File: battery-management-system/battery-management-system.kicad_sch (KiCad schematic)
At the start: 0 parts

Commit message: improve placement
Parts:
- added H1, H2, H3, H4: MountingHole_Pad, MountingHole:MountingHole_6.4mm_M6_Pad, symbol benediktibk:MountingHole_Pad_M6
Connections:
- new net GND: H1.1, H2.1, H3.1, H4.1
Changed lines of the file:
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@@
   (junction (at 68.58 91.44) (diameter 0) (color 0 0 0 0)
   )
+  (wire (pts (xy 236.22 40.64) (xy 236.22 41.91))
+    (stroke (width 0) (type default))
+  )
   (wire (pts (xy 58.42 87.63) (xy 71.12 87.63))
     (stroke (width 0) (type default))
@@
     (stroke (width 0) (type default))
   )
+  (wire (pts (xy 259.08 25.4) (xy 259.08 26.67))
+    (stroke (width 0) (type default))
+  )
   (wire (pts (xy 12.7 83.82) (xy 22.86 83.82))
     (stroke (width 0) (type default))
@@
     (stroke (width 0) (type default))
   )
+  (wire (pts (xy 259.08 40.64) (xy 259.08 41.91))
+    (stroke (width 0) (type default))
+  )
   (wire (pts (xy 78.74 130.81) (xy 106.68 130.81))
     (stroke (width 0) (type default))
@@
     (stroke (width 0) (type default))
   )
+  (wire (pts (xy 236.22 25.4) (xy 236.22 26.67))
+    (stroke (width 0) (type default))
+  )
   (wire (pts (xy 195.58 87.63) (xy 242.57 87.63))
     (stroke (width 0) (type default))
@@
     (effects (font (size 1.27 1.27)) (justify left bottom))
   )
+  (symbol (lib_id "power:GND") (at 236.22 41.91 0) (unit 1)
+    (in_bom yes) (on_board yes) (dnp no) (fields_autoplaced)
+    (property "Reference" "#PWR045" (at 236.22 48.26 0)
+      (effects (font (size 1.27 1.27)) hide)
+    )
+    (property "Value" "GND" (at 236.22 46.99 0)
+      (effects (font (size 1.27 1.27)))
+    )
+    (property "Footprint" "" (at 236.22 41.91 0)
+      (effects (font (size 1.27 1.27)) hide)
+    )
+    (property "Datasheet" "" (at 236.22 41.91 0)
+      (effects (font (size 1.27 1.27)) hide)
+    )
+    (pin "1")
+    (instances
+      (project "battery-management-system"
+        (path "/5272f0ff-3069-41a9-bca2-80beede8b4b2"
+          (reference "#PWR045") (unit 1)
+        )
+      )
+    )
+  )
+  (symbol (lib_id "power:GND") (at 259.08 41.91 0) (unit 1)
+    (in_bom yes) (on_board yes) (dnp no) (fields_autoplaced)
+    (property "Reference" "#PWR047" (at 259.08 48.26 0)
+      (effects (font (size 1.27 1.27)) hide)
+    )
+    (property "Value" "GND" (at 259.08 46.99 0)
+      (effects (font (size 1.27 1.27)))
+    )
+    (property "Footprint" "" (at 259.08 41.91 0)
+      (effects (font (size 1.27 1.27)) hide)
+    )
+    (property "Datasheet" "" (at 259.08 41.91 0)
+      (effects (font (size 1.27 1.27)) hide)
+    )
+    (pin "1")
+    (instances
+      (project "battery-management-system"
+        (path "/5272f0ff-3069-41a9-bca2-80beede8b4b2"
+          (reference "#PWR047") (unit 1)
+        )
+      )
+    )
+  )
+  (symbol (lib_id "benediktibk:MountingHole_Pad_M6") (at 259.08 22.86 0) (unit 1)
+    (in_bom yes) (on_board yes) (dnp no) (fields_autoplaced)
+    (property "Reference" "H3" (at 261.62 20.32 0)
+      (effects (font (size 1.27 1.27)) (justify left))
+    )
+    (property "Value" "MountingHole_Pad" (at 261.62 22.86 0)
+      (effects (font (size 1.27 1.27)) (justify left))
+    )
+    (property "Footprint" "MountingHole:MountingHole_6.4mm_M6_Pad" (at 259.08 22.86 0)
+      (effects (font (size 1.27 1.27)) hide)
+    )
+    (property "Datasheet" "~" (at 259.08 22.86 0)
+      (effects (font (size 1.27 1.27)) hide)
+    )
+    (pin "1")
+    (instances
+      (project "battery-management-system"
+        (path "/5272f0ff-3069-41a9-bca2-80beede8b4b2"
+          (reference "H3") (unit 1)
+        )
+      )
+    )
+  )
+  (symbol (lib_id "benediktibk:MountingHole_Pad_M6") (at 236.22 22.86 0) (unit 1)
+    (in_bom yes) (on_board yes) (dnp no) (fields_autoplaced)
+    (property "Reference" "H1" (at 238.76 20.32 0)
+      (effects (font (size 1.27 1.27)) (justify left))
+    )
+    (property "Value" "MountingHole_Pad" (at 238.76 22.86 0)
+      (effects (font (size 1.27 1.27)) (justify left))
+    )
+    (property "Footprint" "MountingHole:MountingHole_6.4mm_M6_Pad" (at 236.22 22.86 0)
+      (effects (font (size 1.27 1.27)) hide)
+    )
+    (property "Datasheet" "~" (at 236.22 22.86 0)
+      (effects (font (size 1.27 1.27)) hide)
+    )
+    (pin "1")
+    (instances
+      (project "battery-management-system"
+        (path "/5272f0ff-3069-41a9-bca2-80beede8b4b2"
+          (reference "H1") (unit 1)
+        )
+      )
+    )
+  )
+  (symbol (lib_id "power:GND") (at 236.22 26.67 0) (unit 1)
+    (in_bom yes) (on_board yes) (dnp no) (fields_autoplaced)
+    (property "Reference" "#PWR044" (at 236.22 33.02 0)
+      (effects (font (size 1.27 1.27)) hide)
+    )
+    (property "Value" "GND" (at 236.22 31.75 0)
+      (effects (font (size 1.27 1.27)))
+    )
+    (property "Footprint" "" (at 236.22 26.67 0)
+      (effects (font (size 1.27 1.27)) hide)
+    )
+    (property "Datasheet" "" (at 236.22 26.67 0)
+      (effects (font (size 1.27 1.27)) hide)
+    )
+    (pin "1")
+    (instances
+      (project "battery-management-system"
+        (path "/5272f0ff-3069-41a9-bca2-80beede8b4b2"
+          (reference "#PWR044") (unit 1)
+        )
+      )
+    )
+  )
+  (symbol (lib_id "benediktibk:MountingHole_Pad_M6") (at 259.08 38.1 0) (unit 1)
+    (in_bom yes) (on_board yes) (dnp no) (fields_autoplaced)
+    (property "Reference" "H4" (at 261.62 35.56 0)
+      (effects (font (size 1.27 1.27)) (justify left))
+    )
+    (property "Value" "MountingHole_Pad" (at 261.62 38.1 0)
+      (effects (font (size 1.27 1.27)) (justify left))
+    )
+    (property "Footprint" "MountingHole:MountingHole_6.4mm_M6_Pad" (at 259.08 38.1 0)
+      (effects (font (size 1.27 1.27)) hide)
+    )
+    (property "Datasheet" "~" (at 259.08 38.1 0)
+      (effects (font (size 1.27 1.27)) hide)
+    )
+    (pin "1")
+    (instances
+      (project "battery-management-system"
+        (path "/5272f0ff-3069-41a9-bca2-80beede8b4b2"
+          (reference "H4") (unit 1)
+        )
+      )
+    )
+  )
+  (symbol (lib_id "benediktibk:MountingHole_Pad_M6") (at 236.22 38.1 0) (unit 1)
+    (in_bom yes) (on_board yes) (dnp no) (fields_autoplaced)
+    (property "Reference" "H2" (at 238.76 35.56 0)
+      (effects (font (size 1.27 1.27)) (justify left))
+    )
+    (property "Value" "MountingHole_Pad" (at 238.76 38.1 0)
+      (effects (font (size 1.27 1.27)) (justify left))
+    )
+    (property "Footprint" "MountingHole:MountingHole_6.4mm_M6_Pad" (at 236.22 38.1 0)
+      (effects (font (size 1.27 1.27)) hide)
+    )
+    (property "Datasheet" "~" (at 236.22 38.1 0)
+      (effects (font (size 1.27 1.27)) hide)
+    )
+    (pin "1")
+    (instances
+      (project "battery-management-system"
+        (path "/5272f0ff-3069-41a9-bca2-80beede8b4b2"
+          (reference "H2") (unit 1)
+        )
+      )
+    )
+  )
+  (symbol (lib_id "power:GND") (at 259.08 26.67 0) (unit 1)
+    (in_bom yes) (on_board yes) (dnp no) (fields_autoplaced)
+    (property "Reference" "#PWR046" (at 259.08 33.02 0)
+      (effects (font (size 1.27 1.27)) hide)
+    )
+    (property "Value" "GND" (at 259.08 31.75 0)
+      (effects (font (size 1.27 1.27)))
+    )
+    (property "Footprint" "" (at 259.08 26.67 0)
+      (effects (font (size 1.27 1.27)) hide)
+    )
+    (property "Datasheet" "" (at 259.08 26.67 0)
+      (effects (font (size 1.27 1.27)) hide)
+    )
+    (pin "1")
+    (instances
+      (project "battery-management-system"
+        (path "/5272f0ff-3069-41a9-bca2-80beede8b4b2"
+          (reference "#PWR046") (unit 1)
+        )
+      )
+    )
+  )
   (sheet (at 22.86 81.28) (size 35.56 27.94) (fields_autoplaced)

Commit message: finish first draft of layout
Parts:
- removed H4: MountingHole_Pad, MountingHole:MountingHole_6.4mm_M6_Pad, symbol benediktibk:MountingHole_Pad_M6
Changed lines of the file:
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@@
-    (stroke (width 0) (type default))
-  )
-  (wire (pts (xy 259.08 40.64) (xy 259.08 41.91))
     (stroke (width 0) (type default))
   )
@@
     )
   )
-  (symbol (lib_id "power:GND") (at 259.08 41.91 0) (unit 1)
-    (in_bom yes) (on_board yes) (dnp no) (fields_autoplaced)
-    (property "Reference" "#PWR047" (at 259.08 48.26 0)
-      (effects (font (size 1.27 1.27)) hide)
-    )
-    (property "Value" "GND" (at 259.08 46.99 0)
-      (effects (font (size 1.27 1.27)))
-    )
-    (property "Footprint" "" (at 259.08 41.91 0)
-      (effects (font (size 1.27 1.27)) hide)
-    )
-    (property "Datasheet" "" (at 259.08 41.91 0)
-      (effects (font (size 1.27 1.27)) hide)
-    )
-    (pin "1")
-    (instances
-      (project "battery-management-system"
-        (path "/5272f0ff-3069-41a9-bca2-80beede8b4b2"
-          (reference "#PWR047") (unit 1)
-        )
-      )
-    )
-  )
   (symbol (lib_id "benediktibk:MountingHole_Pad_M6") (at 259.08 22.86 0) (unit 1)
     (in_bom yes) (on_board yes) (dnp no) (fields_autoplaced)
@@
         )
       )
-    )
-  )
-  (symbol (lib_id "benediktibk:MountingHole_Pad_M6") (at 259.08 38.1 0) (unit 1)
-    (in_bom yes) (on_board yes) (dnp no) (fields_autoplaced)
-    (property "Reference" "H4" (at 261.62 35.56 0)
-      (effects (font (size 1.27 1.27)) (justify left))
-    )
-    (property "Value" "MountingHole_Pad" (at 261.62 38.1 0)
-      (effects (font (size 1.27 1.27)) (justify left))
-    )
-    (property "Footprint" "MountingHole:MountingHole_6.4mm_M6_Pad" (at 259.08 38.1 0)
-      (effects (font (size 1.27 1.27)) hide)
-    )
-    (property "Datasheet" "~" (at 259.08 38.1 0)
-      (effects (font (size 1.27 1.27)) hide)
-    )
-    (pin "1")
-    (instances
-      (project "battery-management-system"
-        (path "/5272f0ff-3069-41a9-bca2-80beede8b4b2"
-          (reference "H4") (unit 1)
-        )
-      )

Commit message: improve layout
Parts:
- H1, H2, H3: footprint MountingHole:MountingHole_6.4mm_M6_Pad -> benediktibk:MountingHole_6.4mm_M6_Pad_TopBottom
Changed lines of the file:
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@@
   (symbol (lib_id "power:GND") (at 236.22 41.91 0) (unit 1)
     (in_bom yes) (on_board yes) (dnp no) (fields_autoplaced)
-    (property "Reference" "#PWR045" (at 236.22 48.26 0)
+    (property "Reference" "#PWR02" (at 236.22 48.26 0)
       (effects (font (size 1.27 1.27)) hide)
     )
@@
       (project "battery-management-system"
         (path "/5272f0ff-3069-41a9-bca2-80beede8b4b2"
-          (reference "#PWR045") (unit 1)
+          (reference "#PWR02") (unit 1)
         )
       )
@@
       (effects (font (size 1.27 1.27)) (justify left))
     )
-    (property "Footprint" "MountingHole:MountingHole_6.4mm_M6_Pad" (at 259.08 22.86 0)
+    (property "Footprint" "benediktibk:MountingHole_6.4mm_M6_Pad_TopBottom" (at 259.08 22.86 0)
       (effects (font (size 1.27 1.27)) hide)
     )
@@
       (effects (font (size 1.27 1.27)) (justify left))
     )
-    (property "Footprint" "MountingHole:MountingHole_6.4mm_M6_Pad" (at 236.22 22.86 0)
+    (property "Footprint" "benediktibk:MountingHole_6.4mm_M6_Pad_TopBottom" (at 236.22 22.86 0)
       (effects (font (size 1.27 1.27)) hide)
     )
@@
   (symbol (lib_id "power:GND") (at 236.22 26.67 0) (unit 1)
     (in_bom yes) (on_board yes) (dnp no) (fields_autoplaced)
-    (property "Reference" "#PWR044" (at 236.22 33.02 0)
+    (property "Reference" "#PWR01" (at 236.22 33.02 0)
       (effects (font (size 1.27 1.27)) hide)
     )
@@
       (project "battery-management-system"
         (path "/5272f0ff-3069-41a9-bca2-80beede8b4b2"
-          (reference "#PWR044") (unit 1)
+          (reference "#PWR01") (unit 1)
         )
       )
@@
       (effects (font (size 1.27 1.27)) (justify left))
     )
-    (property "Footprint" "MountingHole:MountingHole_6.4mm_M6_Pad" (at 236.22 38.1 0)
+    (property "Footprint" "benediktibk:MountingHole_6.4mm_M6_Pad_TopBottom" (at 236.22 38.1 0)
       (effects (font (size 1.27 1.27)) hide)
     )
@@
   (symbol (lib_id "power:GND") (at 259.08 26.67 0) (unit 1)
     (in_bom yes) (on_board yes) (dnp no) (fields_autoplaced)
-    (property "Reference" "#PWR046" (at 259.08 33.02 0)
+    (property "Reference" "#PWR03" (at 259.08 33.02 0)
       (effects (font (size 1.27 1.27)) hide)
     )
@@
       (project "battery-management-system"
         (path "/5272f0ff-3069-41a9-bca2-80beede8b4b2"
-          (reference "#PWR046") (unit 1)
+          (reference "#PWR03") (unit 1)
         )
       )

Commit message: simplify cell measurement
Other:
- sheet Cell Balancing ports: added none; removed BALANCE_CAP_MINUS_RAW, BALANCE_CAP_PLUS_RAW
- sheet Cell Measurement ports: added none; removed -5V, BALANCE_CAP_MINUS_RAW, BALANCE_CAP_PLUS_RAW
- sheet Power Supply ports: added none; removed -5V
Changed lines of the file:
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@@
-    (stroke (width 0) (type default))
-  )
-  (wire (pts (xy 154.94 34.29) (xy 161.29 34.29))
     (stroke (width 0) (type default))
   )
@@
     (stroke (width 0) (type default))
   )
-  (wire (pts (xy 149.86 134.62) (xy 158.75 134.62))
-    (stroke (width 0) (type default))
-  )
   (wire (pts (xy 58.42 95.25) (xy 66.04 95.25))
     (stroke (width 0) (type default))
@@
     (stroke (width 0) (type default))
   )
-  (wire (pts (xy 149.86 138.43) (xy 158.75 138.43))
-    (stroke (width 0) (type default))
-  )
   (wire (pts (xy 12.7 87.63) (xy 22.86 87.63))
     (stroke (width 0) (type default))
@@
     (stroke (width 0) (type default))
   )
-  (wire (pts (xy 74.93 83.82) (xy 97.79 83.82))
-    (stroke (width 0) (type default))
-  )
   (wire (pts (xy 63.5 99.06) (xy 97.79 99.06))
     (stroke (width 0) (type default))
@@
     (stroke (width 0) (type default))
   )
-  (wire (pts (xy 72.39 110.49) (xy 97.79 110.49))
-    (stroke (width 0) (type default))
-  )
   (wire (pts (xy 106.68 146.05) (xy 71.12 146.05))
     (stroke (width 0) (type default))
@@
     (stroke (width 0) (type default))
   )
-  (wire (pts (xy 72.39 106.68) (xy 97.79 106.68))
-    (stroke (width 0) (type default))
-  )
   (wire (pts (xy 78.74 172.72) (xy 106.68 172.72))
     (stroke (width 0) (type default))
@@
     (effects (font (size 1.27 1.27)) (justify left bottom))
   )
-  (label "-5V" (at 74.93 83.82 0) (fields_autoplaced)
-    (effects (font (size 1.27 1.27)) (justify left bottom))
-  )
   (label "CHARGE" (at 12.7 83.82 0) (fields_autoplaced)
     (effects (font (size 1.27 1.27)) (justify left bottom))
@@
     (effects (font (size 1.27 1.27)) (justify left bottom))
   )
-  (label "-5V" (at 161.29 34.29 0) (fields_autoplaced)
-    (effects (font (size 1.27 1.27)) (justify left bottom))
-  )
   (label "EN_CELL_BALANCING" (at 78.74 142.24 0) (fields_autoplaced)
     (effects (font (size 1.27 1.27)) (justify left bottom))
@@
     (effects (font (size 1.27 1.27)) (justify left bottom))
   )
-  (label "BALANCE_CAP_MINUS_RAW" (at 158.75 138.43 0) (fields_autoplaced)
-    (effects (font (size 1.27 1.27)) (justify left bottom))
-  )
-  (label "BALANCE_CAP_PLUS_RAW" (at 72.39 106.68 0) (fields_autoplaced)
-    (effects (font (size 1.27 1.27)) (justify left bottom))
-  )
   (label "18V" (at 78.74 130.81 0) (fields_autoplaced)
     (effects (font (size 1.27 1.27)) (justify left bottom))
@@
     (effects (font (size 1.27 1.27)) (justify left bottom))
   )
-  (label "BALANCE_CAP_MINUS_RAW" (at 72.39 110.49 0) (fields_autoplaced)
-    (effects (font (size 1.27 1.27)) (justify left bottom))
-  )
   (label "5V" (at 161.29 30.48 0) (fields_autoplaced)
-    (effects (font (size 1.27 1.27)) (justify left bottom))
-  )
-  (label "BALANCE_CAP_PLUS_RAW" (at 158.75 134.62 0) (fields_autoplaced)
     (effects (font (size 1.27 1.27)) (justify left bottom))
   )
@@
       (effects (font (size 1.27 1.27)) (justify left))
     )
-    (pin "BALANCE_CAP_MINUS_RAW" output (at 149.86 138.43 0)
-      (effects (font (size 1.27 1.27)) (justify right))
-    )
-    (pin "BALANCE_CAP_PLUS_RAW" output (at 149.86 134.62 0)
-      (effects (font (size 1.27 1.27)) (justify right))
-    )
     (pin "SELECT_A0" input (at 106.68 168.91 180)
       (effects (font (size 1.27 1.27)) (justify left))
@@
       (effects (font (size 1.27 1.27)) (justify right))
     )
-    (pin "BALANCE_CAP_PLUS_RAW" input (at 97.79 106.68 180)
-      (effects (font (size 1.27 1.27)) (justify left))
-    )
-    (pin "BALANCE_CAP_MINUS_RAW" input (at 97.79 110.49 180)
-      (effects (font (size 1.27 1.27)) (justify left))
-    )
     (pin "BALANCE_CAP_PLUS" output (at 138.43 95.25 0)
       (effects (font (size 1.27 1.27)) (justify right))
@@
     )
     (pin "CELL1_MINUS" input (at 97.79 102.87 180)
-      (effects (font (size 1.27 1.27)) (justify left))
-    )
-    (pin "-5V" input (at 97.79 83.82 180)
       (effects (font (size 1.27 1.27)) (justify left))
     )
@@
       (effects (font (size 1.27 1.27)) (justify left))
     )
-    (pin "-5V" output (at 154.94 34.29 0)
-      (effects (font (size 1.27 1.27)) (justify right))
-    )
     (pin "18V" output (at 154.94 38.1 0)

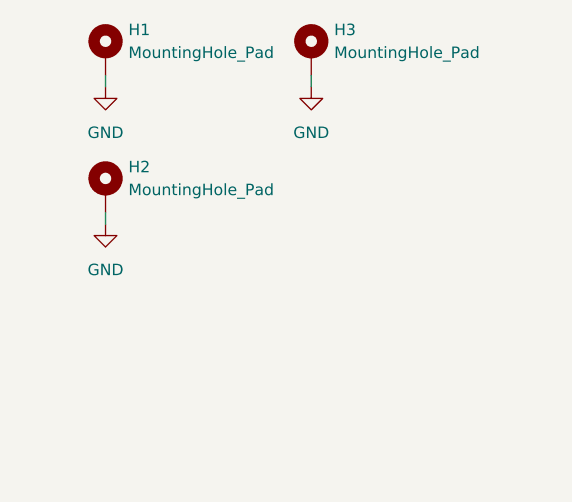
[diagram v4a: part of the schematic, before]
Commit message: develop inductance based balance methods
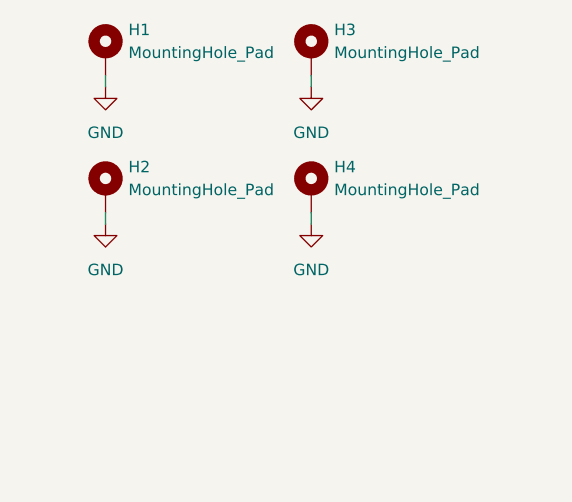
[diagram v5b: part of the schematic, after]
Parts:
- added H4: MountingHole_Pad, benediktibk:MountingHole_6.4mm_M6_Pad_TopBottom, symbol benediktibk:MountingHole_Pad_M6
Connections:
- net GND: now also H4.1
